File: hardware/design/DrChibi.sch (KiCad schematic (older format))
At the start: 19 parts, among them P1 CONN_02X05, P2 PAD_SMD, P3 IN+, P4 IN-, P5 CONN_01X04, X1 MINI-USB-SHIELD-32005-201

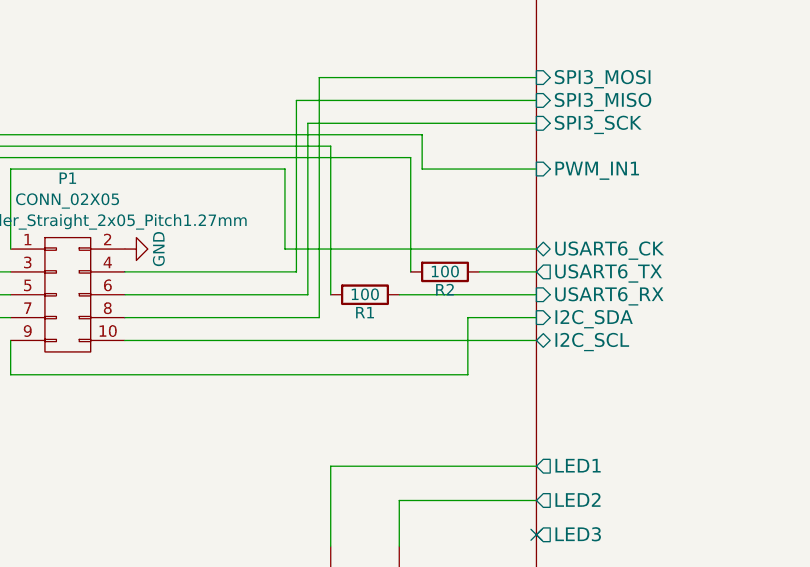
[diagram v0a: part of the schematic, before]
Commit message: TODO Double-check BOM. Check silk screen. Check Gerber output.
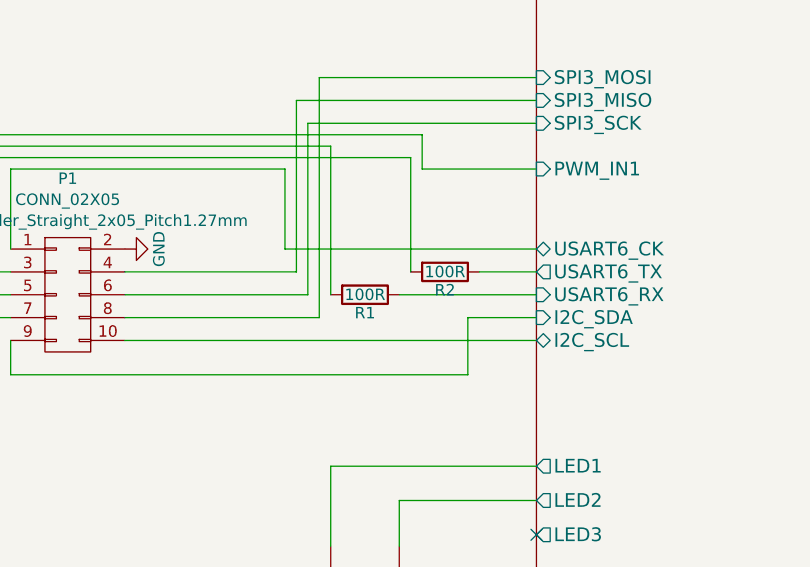
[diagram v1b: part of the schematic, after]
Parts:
- Dusb1: Manufacturer (none) -> NXP; Part Number (none) -> BAT46WH
- P5: Manufacturer (none) -> Molex; Part Number (none) -> PicoBlade 53261-0471
- R1, R2: value 100 -> 100R
- X1: Manufacturer (none) -> Cypress Industries; Part Number (none) -> CCMUSBB-32005-201
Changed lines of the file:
@@
 F 2 "CRF1:mini_USB_gnd" H 1150 2150 50  0001 C CNN
 F 3 "" H 1150 2000 60  0001 C CNN
+F 4 "Cypress Industries" H 1150 2000 60  0001 C CNN "Manufacturer"
+F 5 "CCMUSBB-32005-201" H 1150 2000 60  0001 C CNN "Part Number"
 	1    1150 2000
 	-1   0    0    -1
@@
 P 2750 4300
 F 0 "R2" V 2830 4300 50  0000 C CNN
-F 1 "100" V 2750 4300 50  0000 C CNN
+F 1 "100R" V 2750 4300 50  0000 C CNN
 F 2 "Resistors_SMD:R_0603" V 2680 4300 30  0001 C CNN
 F 3 "" H 2750 4300 30  0000 C CNN
@@
 P 2400 4400
 F 0 "R1" V 2480 4400 50  0000 C CNN
-F 1 "100" V 2400 4400 50  0000 C CNN
+F 1 "100R" V 2400 4400 50  0000 C CNN
 F 2 "Resistors_SMD:R_0603" V 2330 4400 30  0001 C CNN
 F 3 "" H 2400 4400 30  0000 C CNN
@@
 F 2 "Diodes_SMD:SOD-123" H 2300 1700 60  0001 C CNN
 F 3 "" H 2300 1700 60  0000 C CNN
+F 4 "NXP" H 2300 1700 60  0001 C CNN "Manufacturer"
+F 5 "BAT46WH" H 2300 1700 60  0001 C CNN "Part Number"
 	1    2300 1700
 	-1   0    0    -1
@@
 F 2 "Connectors_Molex:Connector_Molex_PicoBlade_53261-0471" H 619 2560 50  0000 C CNN
 F 3 "" H 700 2850 50  0000 C CNN
+F 4 "Molex" H 700 2850 60  0001 C CNN "Manufacturer"
+F 5 "PicoBlade 53261-0471" H 700 2850 60  0001 C CNN "Part Number"
 	1    700  2850
 	-1   0    0    1

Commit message: Added "just-in-case-" pads at PWM d,e,f.
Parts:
- added P_PWM1, P_PWM2, P_PWM3: PAD_SMD, Pads:PAD_SMD_1x1, symbol PAD_SMD
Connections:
- net Half Bridge D/PWM: now also P_PWM1.1 (PAD)
- net Half Bridge E/PWM: now also P_PWM2.1 (PAD)
- net Half Bridge F/PWM: now also P_PWM3.1 (PAD)
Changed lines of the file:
@@
 	9450 5800 9750 5800
 NoConn ~ 3150 5450
+$Comp
+L PAD_SMD P_PWM1
+U 1 1 57CE1BCB
+P 7750 4500
+F 0 "P_PWM1" H 7878 4553 60  0000 L CNN
+F 1 "PAD_SMD" H 7878 4447 60  0000 L CNN
+F 2 "Pads:PAD_SMD_1x1" H 7750 4250 60  0001 C CNN
+F 3 "" H 7750 4350 60  0000 C CNN
+	1    7750 4500
+	1    0    0    -1
+$EndComp
+$Comp
+L PAD_SMD P_PWM2
+U 1 1 57CE1E7F
+P 7750 5400
+F 0 "P_PWM2" H 7878 5453 60  0000 L CNN
+F 1 "PAD_SMD" H 7878 5347 60  0000 L CNN
+F 2 "Pads:PAD_SMD_1x1" H 7750 5150 60  0001 C CNN
+F 3 "" H 7750 5250 60  0000 C CNN
+	1    7750 5400
+	1    0    0    -1
+$EndComp
+$Comp
+L PAD_SMD P_PWM3
+U 1 1 57CE2131
+P 7750 6300
+F 0 "P_PWM3" H 7878 6353 60  0000 L CNN
+F 1 "PAD_SMD" H 7878 6247 60  0000 L CNN
+F 2 "Pads:PAD_SMD_1x1" H 7750 6050 60  0001 C CNN
+F 3 "" H 7750 6150 60  0000 C CNN
+	1    7750 6300
+	1    0    0    -1
+$EndComp
+Wire Wire Line
+	7550 4500 5850 4500
+Wire Wire Line
+	5850 4500 5850 3800
+Connection ~ 5850 3800
+Wire Wire Line
+	7550 5400 5850 5400
+Wire Wire Line
+	5850 5400 5850 4700
+Connection ~ 5850 4700
+Wire Wire Line
+	7550 6300 5850 6300
+Wire Wire Line
+	5850 6300 5850 5600
+Connection ~ 5850 5600
 $EndSCHEMATC

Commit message: Swapped STM32 Pin33 and Pin50 and added some pads to enable usage of USART3 when TIM8 is bridged to PWM d,e,f.
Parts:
- added P_PWM4, P_PWM5, P_USART3_CLK1: PAD_SMD, Pads:PAD_SMD_1x1, symbol PAD_SMD
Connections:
- net Half Bridge D/PWM: now also P_PWM4.1 (PAD)
- net Half Bridge E/PWM: now also P_PWM5.1 (PAD)
- net MCU/LED3: now also P_USART3_CLK1.1 (PAD)
- no-connect marks 2 -> 1
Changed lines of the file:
@@
 Wire Wire Line
 	9450 5800 9750 5800
-NoConn ~ 3150 5450
 $Comp
 L PAD_SMD P_PWM1
@@
 	5850 6300 5850 5600
 Connection ~ 5850 5600
+$Comp
+L PAD_SMD P_PWM4
+U 1 1 57CDF36C
+P 7750 4750
+F 0 "P_PWM4" H 7878 4803 60  0000 L CNN
+F 1 "PAD_SMD" H 7878 4697 60  0000 L CNN
+F 2 "Pads:PAD_SMD_1x1" H 7750 4500 60  0001 C CNN
+F 3 "" H 7750 4600 60  0000 C CNN
+	1    7750 4750
+	1    0    0    -1
+$EndComp
+$Comp
+L PAD_SMD P_PWM5
+U 1 1 57CDF8FA
+P 7750 5650
+F 0 "P_PWM5" H 7878 5703 60  0000 L CNN
+F 1 "PAD_SMD" H 7878 5597 60  0000 L CNN
+F 2 "Pads:PAD_SMD_1x1" H 7750 5400 60  0001 C CNN
+F 3 "" H 7750 5500 60  0000 C CNN
+	1    7750 5650
+	1    0    0    -1
+$EndComp
+Wire Wire Line
+	7550 4750 7500 4750
+Wire Wire Line
+	7500 4750 7500 4500
+Connection ~ 7500 4500
+Wire Wire Line
+	7550 5650 7500 5650
+Wire Wire Line
+	7500 5650 7500 5400
+Connection ~ 7500 5400
+$Comp
+L PAD_SMD P_USART3_CLK1
+U 1 1 57CE2827
+P 2850 5450
+F 0 "P_USART3_CLK1" H 2794 5163 60  0000 C CNN
+F 1 "PAD_SMD" H 2794 5269 60  0000 C CNN
+F 2 "Pads:PAD_SMD_1x1" H 2850 5200 60  0001 C CNN
+F 3 "" H 2850 5300 60  0000 C CNN
+	1    2850 5450
+	-1   0    0    1
+$EndComp
+Wire Wire Line
+	3050 5450 3150 5450
 $EndSCHEMATC
